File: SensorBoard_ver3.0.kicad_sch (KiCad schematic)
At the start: 43 parts, among them IC1 MIC5504-3.3YM5-T5, J1 STLink, SW1 CAN_Terminal, SW2 IDSetSW, SW3 Reset, SW4 IDSetSW, U1 L7805, U2 MAX3485, U3 ATA6561, U4 STM32F303K8Tx, Y1 Crystal

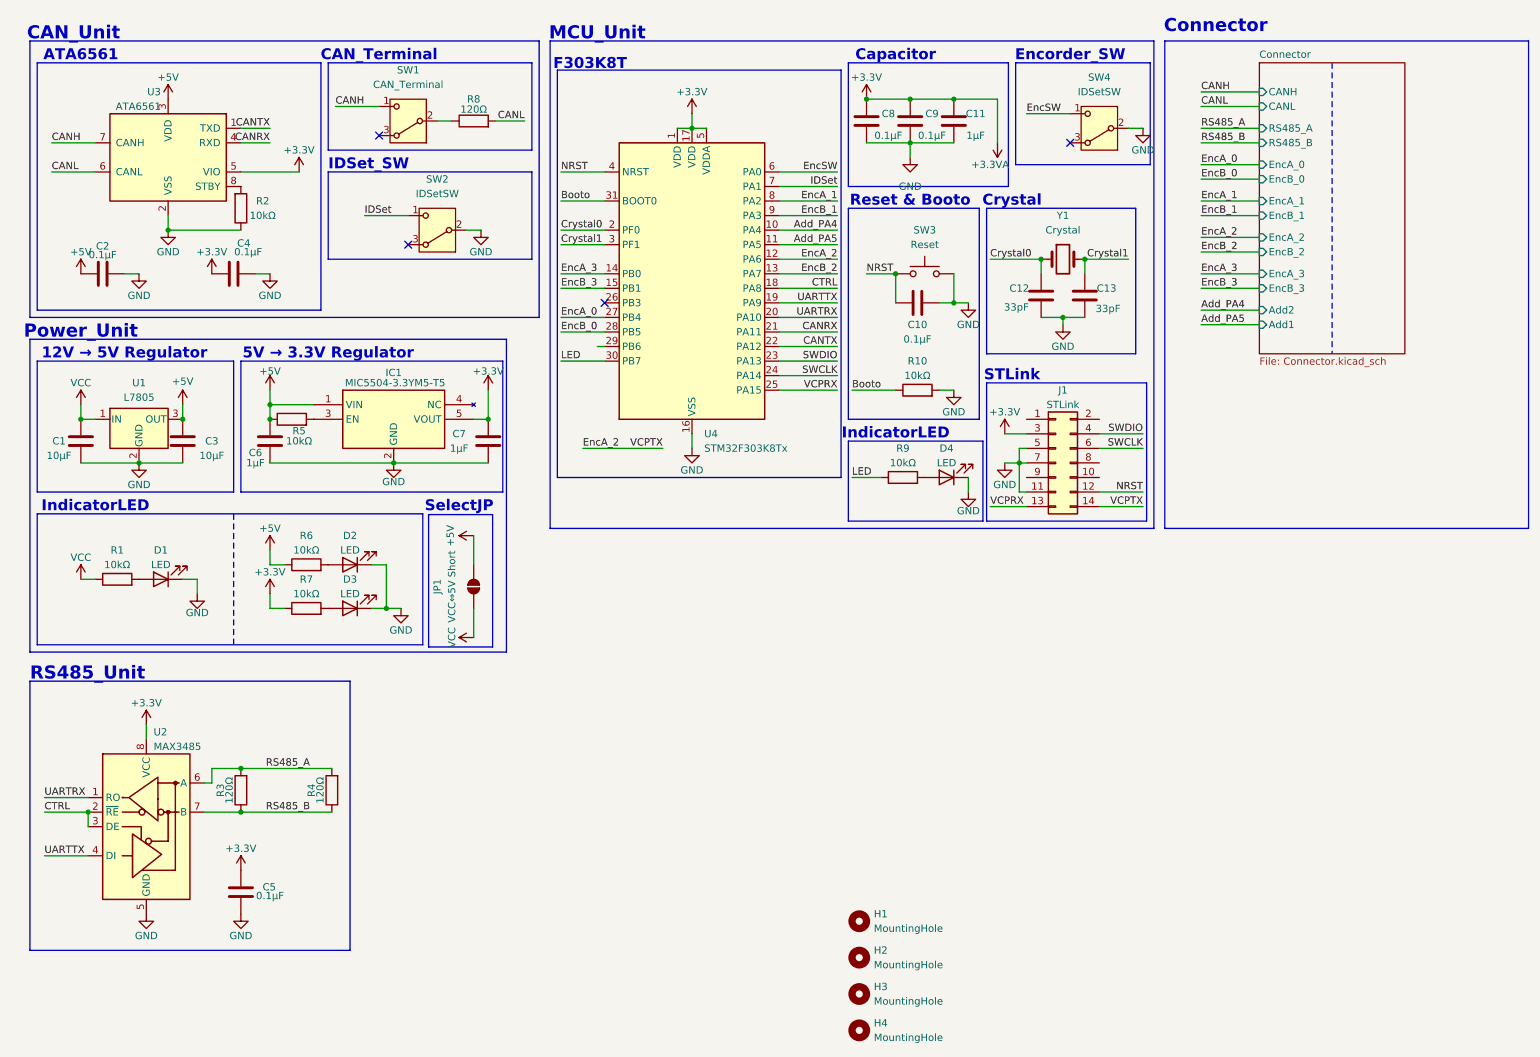
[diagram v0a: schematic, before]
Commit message: コネクタを縦向きにする工事の前のコミット
コネクタを縦向きにする可能性が出てきたので、失敗したときのバックアップのためのコミット
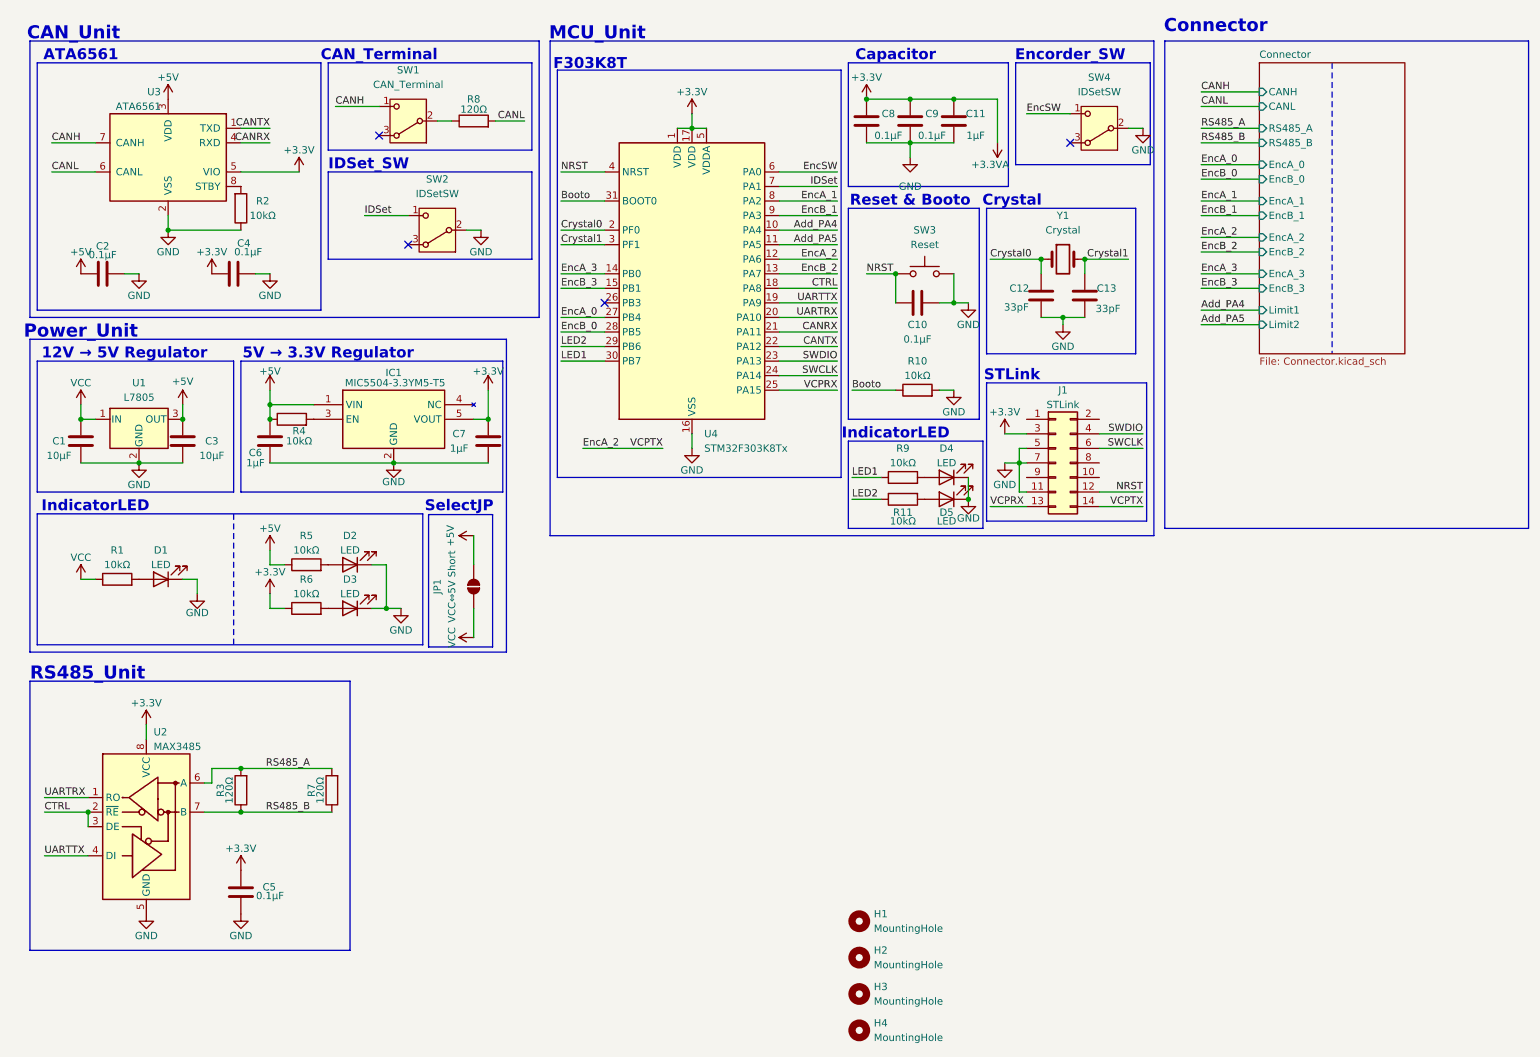
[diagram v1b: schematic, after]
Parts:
- added D5: LED, LED_SMD:LED_0603_1608Metric, symbol Device:LED
- added R11: 10kΩ, Resistor_SMD:R_0603_1608Metric, symbol Device:R
- renumbered R5 to R4, R6 to R5, R7 to R6, R4 to R7
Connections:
- net GND: now also D5.1 (K)
- net LED2: now reaches U4.29 (PB6)
- net LED2: now also R11.1
- net LED renamed LED1
- new net: D5.2 (A), R11.2
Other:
- sheet Connector ports: added Limit1, Limit2; removed Add1, Add2
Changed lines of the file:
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@@
 	(rectangle
 		(start 156.845 87.63)
-		(end 180.34 101.6)
+		(end 180.34 102.87)
 		(stroke
 			(width 0)
@@
 	(rectangle
 		(start 104.775 17.78)
-		(end 210.185 102.87)
+		(end 210.185 104.14)
 		(stroke
 			(width 0)
@@
 	)
 	(junction
+		(at 177.8 97.79)
+		(diameter 0)
+		(color 0 0 0 0)
+	)
+	(junction
 		(at 50.8 152.4)
 		(diameter 0)
@@
 	(wire
 		(pts
-			(xy 177.8 96.52) (xy 177.8 93.98)
+			(xy 177.8 97.79) (xy 177.8 93.98)
 		)
 		(stroke
@@
 	(wire
 		(pts
+			(xy 106.68 71.12) (xy 114.3 71.12)
+		)
+		(stroke
+			(width 0)
+			(type default)
+		)
+	)
+	(wire
+		(pts
 			(xy 55.88 33.02) (xy 50.8 33.02)
 		)
@@
 	(wire
 		(pts
-			(xy 113.03 71.12) (xy 114.3 71.12)
+			(xy 44.45 147.32) (xy 45.72 147.32)
 		)
 		(stroke
@@
 	(wire
 		(pts
-			(xy 44.45 147.32) (xy 45.72 147.32)
+			(xy 129.54 86.36) (xy 129.54 88.9)
 		)
 		(stroke
@@
 	(wire
 		(pts
-			(xy 129.54 86.36) (xy 129.54 88.9)
+			(xy 186.69 91.44) (xy 187.96 91.44)
 		)
 		(stroke
@@
 	(wire
 		(pts
-			(xy 186.69 91.44) (xy 187.96 91.44)
+			(xy 34.29 137.16) (xy 34.29 139.7)
 		)
 		(stroke
@@
 	(wire
 		(pts
-			(xy 34.29 137.16) (xy 34.29 139.7)
+			(xy 55.88 78.74) (xy 55.88 81.28)
 		)
 		(stroke
@@
 	(wire
 		(pts
-			(xy 55.88 78.74) (xy 55.88 81.28)
+			(xy 218.44 39.37) (xy 228.6 39.37)
 		)
 		(stroke
@@
 	(wire
 		(pts
-			(xy 218.44 39.37) (xy 228.6 39.37)
+			(xy 157.48 97.79) (xy 162.56 97.79)
 		)
 		(stroke
@@
 		)
 	)
-	(label "LED"
+	(label "LED1"
 		(at 157.48 93.98 0)
 		(effects
@@
 		)
 	)
+	(label "LED2"
+		(at 106.68 71.12 0)
+		(effects
+			(font
+				(size 1.27 1.27)
+			)
+			(justify left bottom)
+		)
+	)
 	(label "EncB_0"
 		(at 106.68 68.58 0)
@@
 		)
 	)
-	(label "LED"
+	(label "LED1"
 		(at 106.68 73.66 0)
 		(effects
@@
 		)
 	)
+	(label "LED2"
+		(at 157.48 97.79 0)
+		(effects
+			(font
+				(size 1.27 1.27)
+			)
+			(justify left bottom)
+		)
+	)
 	(label "VCPTX"
 		(at 208.28 99.06 180)
@@
 		(on_board yes)
 		(dnp no)
-		(property "Reference" "R4"
+		(property "Reference" "R7"
 			(at 63.119 148.59 90)
 			(effects
@@
 			(project "SensorBoard_ver2.0"
 				(path "/48207ddc-a67e-4dc5-8222-aef69eda58f7"
-					(reference "R4")
+					(reference "R7")
 					(unit 1)
 				)
@@
 		(on_board yes)
 		(dnp no)
-		(property "Reference" "R7"
+		(property "Reference" "R6"
 			(at 62.23 111.76 90)
 			(effects
@@
 			(project "SensorBoard_ver2.0"
 				(path "/48207ddc-a67e-4dc5-8222-aef69eda58f7"
-					(reference "R7")
+					(reference "R6")
 					(unit 1)
 				)
@@
 		(on_board yes)
 		(dnp no)
-		(property "Reference" "R5"
+		(property "Reference" "R4"
 			(at 60.96 85.852 90)
 			(effects
@@
 			(project "SensorBoard_ver2.0"
 				(path "/48207ddc-a67e-4dc5-8222-aef69eda58f7"
-					(reference "R5")
+					(reference "R4")
 					(unit 1)
 				)
@@
 	)
 	(symbol
+		(lib_id "Device:R")
+		(at 166.37 97.79 90)
+		(mirror x)
+		(unit 1)
+		(exclude_from_sim no)
+		(in_bom yes)
+		(on_board yes)
+		(dnp no)
+		(property "Reference" "R11"
+			(at 166.37 100.076 90)
+			(effects
+				(font
+					(size 1.27 1.27)
+				)
+			)
+		)
+		(property "Value" "10kΩ"
+			(at 166.37 101.6 90)
+			(effects
+				(font
+					(size 1.27 1.27)
+				)
+			)
+		)
+		(property "Footprint" "Resistor_SMD:R_0603_1608Metric"
+			(at 166.37 96.012 90)
+			(effects
+				(font
+					(size 1.27 1.27)
+				)
+				(hide yes)
+			)
+		)
+		(property "Datasheet" "~"
+			(at 166.37 97.79 0)
+			(effects
+				(font
+					(size 1.27 1.27)
+				)
+				(hide yes)
+			)
+		)
+		(property "Description" "Resistor"
+			(at 166.37 97.79 0)
+			(effects
+				(font
+					(size 1.27 1.27)
+				)
+				(hide yes)
+			)
+		)
+		(pin "1"
+		)
+		(pin "2"
+		)
+		(instances
+			(project "SensorBoard_ver3.0"
+				(path "/48207ddc-a67e-4dc5-8222-aef69eda58f7"
+					(reference "R11")
+					(unit 1)
+				)
+			)
+		)
+	)
+	(symbol
 		(lib_id "Device:C")
 		(at 49.53 58.42 90)
@@
 		(on_board yes)
 		(dnp no)
-		(property "Reference" "R6"
+		(property "Reference" "R5"
 			(at 62.23 104.14 90)
 			(effects
@@
 			(project "SensorBoard_ver2.0"
 				(path "/48207ddc-a67e-4dc5-8222-aef69eda58f7"
-					(reference "R6")
+					(reference "R5")
 					(unit 1)
 				)
@@
 	)
 	(symbol
+		(lib_id "Device:LED")
+		(at 173.99 97.79 180)
+		(unit 1)
+		(exclude_from_sim no)
+		(in_bom yes)
+		(on_board yes)
+		(dnp no)
+		(property "Reference" "D5"
+			(at 173.99 100.076 0)
+			(effects
+				(font
+					(size 1.27 1.27)
+				)
+			)
+		)
+		(property "Value" "LED"
+			(at 173.99 101.6 0)
+			(effects
+				(font
+					(size 1.27 1.27)
+				)
+			)
+		)
+		(property "Footprint" "LED_SMD:LED_0603_1608Metric"
+			(at 173.99 97.79 0)
+			(effects
+				(font
+					(size 1.27 1.27)
+				)
+				(hide yes)
+			)
+		)
+		(property "Datasheet" "~"
+			(at 173.99 97.79 0)
+			(effects
+				(font
+					(size 1.27 1.27)
+				)
+				(hide yes)
+			)
+		)
+		(property "Description" "Light emitting diode"
+			(at 173.99 97.79 0)
+			(effects
+				(font
+					(size 1.27 1.27)
+				)
+				(hide yes)
+			)
+		)
+		(property "Sim.Pins" "1=K 2=A"
+			(at 173.99 97.79 0)
+			(effects
+				(font
+					(size 1.27 1.27)
+				)
+				(hide yes)
+			)
+		)
+		(pin "1"
+		)
+		(pin "2"
+		)
+		(instances
+			(project "SensorBoard_ver3.0"
+				(path "/48207ddc-a67e-4dc5-8222-aef69eda58f7"
+					(reference "D5")
+					(unit 1)
+				)
+			)
+		)
+	)
+	(symbol
 		(lib_id "Device:C")
 		(at 198.12 62.23 0)
@@
 	(symbol
 		(lib_id "power:GND")
-		(at 177.8 96.52 0)
+		(at 177.8 97.79 0)
 		(unit 1)
 		(exclude_from_sim no)
@@
 		(dnp no)
 		(property "Reference" "#PWR032"
-			(at 177.8 102.87 0)
+			(at 177.8 104.14 0)
 			(effects
 				(font
@@
 		)
 		(property "Value" "GND"
-			(at 177.8 99.822 0)
+			(at 177.8 101.092 0)
 			(effects
 				(font
@@
 		)
 		(property "Footprint" ""
-			(at 177.8 96.52 0)
+			(at 177.8 97.79 0)
 			(effects
 				(font
@@
 		)
 		(property "Datasheet" ""
-			(at 177.8 96.52 0)
+			(at 177.8 97.79 0)
 			(effects
 				(font
@@
 		)
 		(property "Description" "Power symbol creates a global label with name \"GND\" , ground"
-			(at 177.8 96.52 0)
+			(at 177.8 97.79 0)
 			(effects
 				(font
@@
 			)
 		)
-		(pin "Add2" input
+		(pin "Limit1" input
 			(at 228.6 64.77 180)
 			(effects
@@
 			)
 		)
-		(pin "Add1" input
+		(pin "Limit2" input
 			(at 228.6 67.31 180)
 			(effects

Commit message: プロジェクトライブラリの追加・多少の進展
・プロジェクトライブラリで三端子レギュレータのフットプリントを管理した
・多少、アートワーク進めた
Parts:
- IC1: footprint SOT95P280X130-5N:SOT95P280X130-5N -> SensorBoard_ver3.0:MIC5504-3.3YM5-T5
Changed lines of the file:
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@@
 			)
 		)
-		(property "Footprint" "SOT95P280X130-5N:SOT95P280X130-5N"
+		(property "Footprint" "SensorBoard_ver3.0:MIC5504-3.3YM5-T5"
 			(at 87.63 176.2 0)
 			(effects
